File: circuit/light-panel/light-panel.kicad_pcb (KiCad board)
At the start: 2 copper layers, 45 x 20 mm, 32 parts, among them J1 Screw_Terminal_01x02, M2 MountingHole

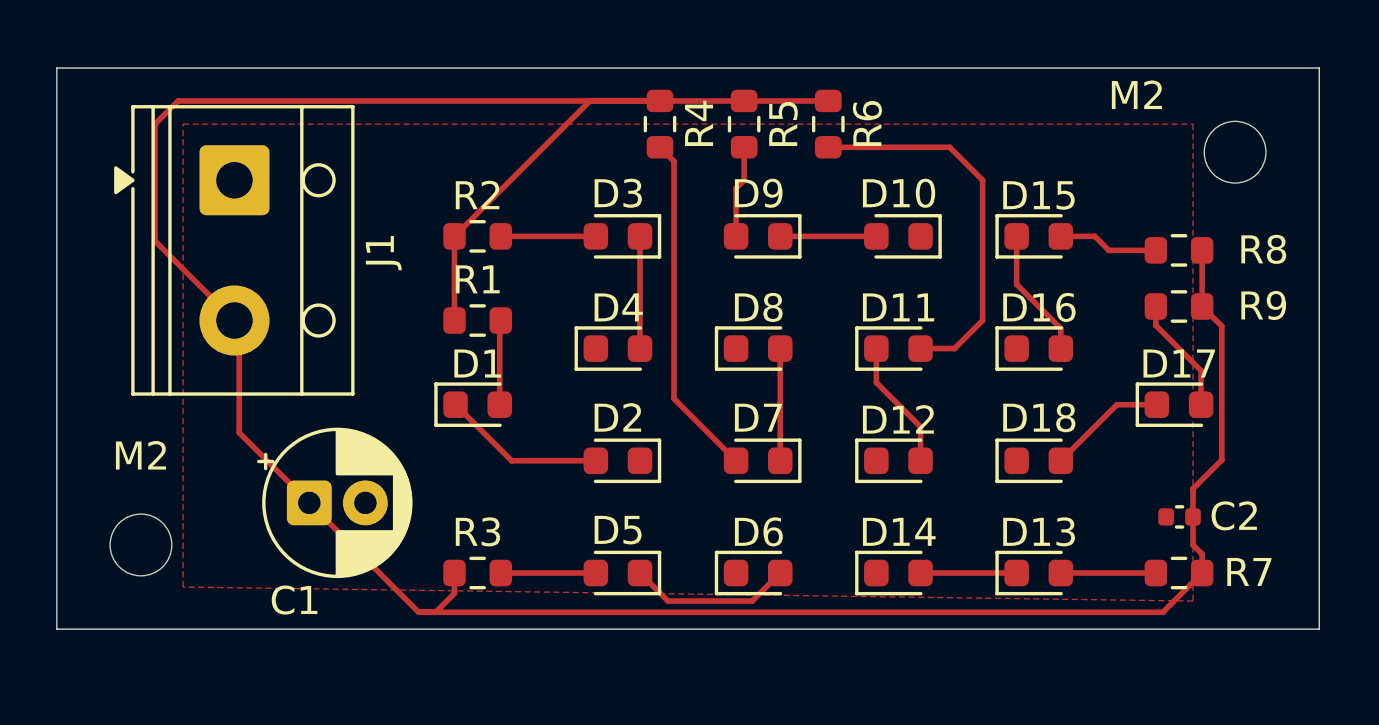
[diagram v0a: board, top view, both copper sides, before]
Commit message: rearrage leds
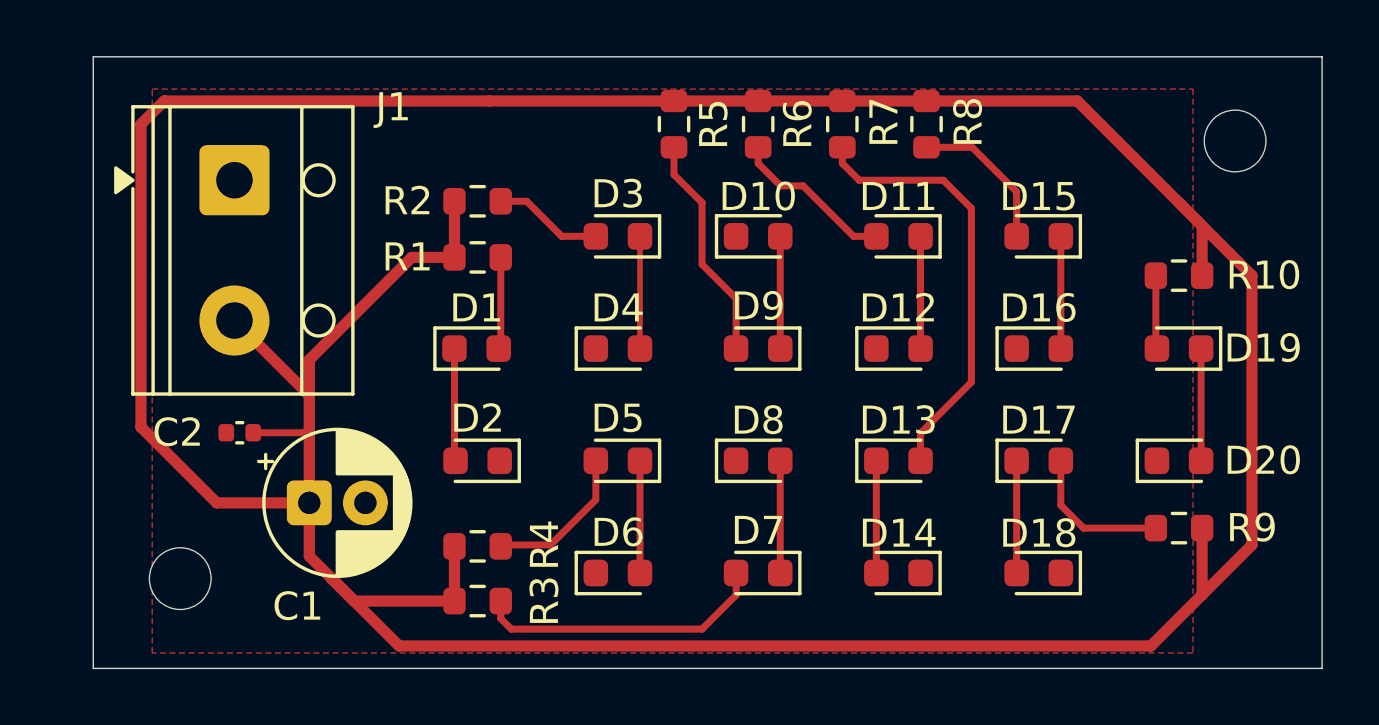
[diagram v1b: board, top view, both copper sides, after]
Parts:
- added D19: KT-0603R, LED_SMD:LED_0603_1608Metric, F.Cu at (124.0, 104.0)
- added D20: KT-0603R, LED_SMD:LED_0603_1608Metric, F.Cu at (124.0, 108.0)
- added R10: 330Ω, Resistor_SMD:R_0603_1608Metric, F.Cu at (124.0, 101.4)
- moved C2 33.6 mm to (90.5, 107.0)
- moved R7 20.0 mm to (112.0, 96.0), turned to -90 degrees
- moved R4 18.2 mm to (99.0, 113.0), turned to 0 degrees
- moved R8 10.1 mm to (115.0, 96.0), turned to -90 degrees
- moved R9 7.90 mm to (124.0, 110.4)
- moved D13 6.40 mm to (114.0, 108.0)
- moved D17 5.39 mm to (119.0, 108.0)
- moved D10 5.00 mm to (109.0, 100.0), turned to 0 degrees
- moved D2 5.00 mm to (99.0, 108.0)
- moved D6 5.00 mm to (104.0, 112.0)
- moved D11 4.00 mm to (114.0, 100.0), turned to 180 degrees
- moved D12 4.00 mm to (114.0, 104.0)
- moved D18 4.00 mm to (119.0, 112.0), turned to 180 degrees
- moved D5 4.00 mm to (104.0, 108.0)
- moved D7 4.00 mm to (109.0, 112.0)
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- renumbered M2 to H1, M2 to H2
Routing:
- net +5V: track 101.1 -> 140.0 mm
- net Net-(D13-A): track 3.39 -> 15.6 mm
- net Net-(D11-A): track 13.6 -> 5.86 mm
- net Net-(D9-A): track 3.29 -> 8.09 mm
- net Net-(D19-K): track 0.00 -> 4.00 mm
- net Net-(D19-A): track 0.00 -> 2.62 mm
- net Net-(D5-A): track 3.39 -> 5.46 mm
- net Net-(D15-A): track 3.59 -> 5.46 mm
- net Net-(D7-A): track 12.3 -> 10.5 mm
- net Net-(D5-K): track 5.83 -> 4.00 mm
- net Net-(D1-K): track 5.83 -> 4.02 mm
- net Net-(D17-A): track 4.17 -> 5.31 mm
- net Net-(D15-K): track 4.65 -> 4.00 mm
- net Net-(D11-K): track 4.65 -> 4.00 mm
- net Net-(D13-K): track 3.43 -> 4.00 mm
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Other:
- board size 45 x 20 mm -> 43.8 x 21.8 mm

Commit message: rearrange leds
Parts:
- added TP1: TestPoint_Probe, TestPoint:TestPoint_THTPad_1.0x1.0mm_Drill0.5mm, F.Cu at (104.0, 96.8)
- added TP2: TestPoint_Probe, TestPoint:TestPoint_THTPad_1.0x1.0mm_Drill0.5mm, F.Cu at (127.8, 101.0)
- added TP3: TestPoint_Probe, TestPoint:TestPoint_THTPad_1.0x1.0mm_Drill0.5mm, F.Cu at (121.6, 106.0)
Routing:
- net Net-(D3-K): track 4.21 -> 7.74 mm
- net +5V: track 140.0 -> 141.3 mm
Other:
- board text added: "Current consumption 5mA x 20 LEDs = 100mA"
- board text added: "Designed by Tam"
- board text added: "TP1"
- board text added: "TP1: Voltage accross 1 LED -> 1.7V TP2: VCC at far side -> 5V TP3: GND"
- board text added: "TP2"
- board text added: "TP3"
